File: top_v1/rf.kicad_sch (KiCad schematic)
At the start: 3 parts

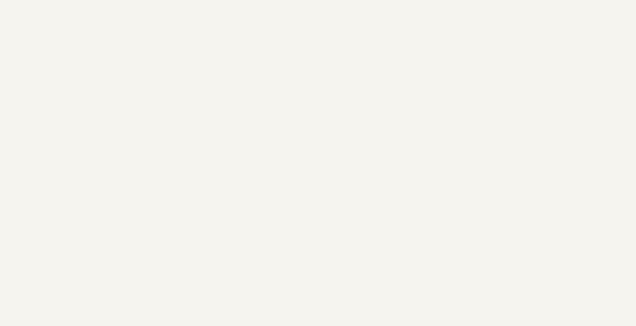
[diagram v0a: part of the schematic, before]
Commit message: File structure enhanced.
Added uniform titleblocks and 3D renders for easier view, file cleanups.
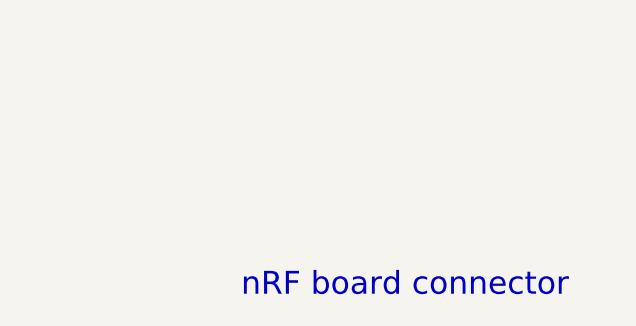
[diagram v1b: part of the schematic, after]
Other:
- note added: "nRF board connector"
- title: (none) -> Top board - nRF and IMU to Nucleo H755ZI
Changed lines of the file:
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@@
 (kicad_sch
-	(version 20231120)
+	(version 20250114)
 	(generator "eeschema")
-	(generator_version "8.0")
+	(generator_version "9.0")
 	(paper "A4")
+	(title_block
+		(title "Top board - nRF and IMU to Nucleo H755ZI")
+		(date "16-12-2024")
+		(rev "1")
+	)
+	(text "nRF board connector"
+		(exclude_from_sim no)
+		(at 209.55 170.18 0)
+		(effects
+			(font
+				(size 2.54 2.54)
+			)
+		)
+	)
 	(junction
 		(at 175.26 81.28)
@@
 	(label "GND"
 		(at 175.26 83.82 0)
-		(fields_autoplaced yes)
 		(effects
 			(font
@@
 		(shape input)
 		(at 164.465 89.535 0)
-		(fields_autoplaced yes)
 		(effects
 			(font
@@
 		(shape input)
 		(at 164.465 86.995 0)
-		(fields_autoplaced yes)
 		(effects
 			(font
@@
 		(shape input)
 		(at 164.465 84.455 0)
-		(fields_autoplaced yes)
 		(effects
 			(font
@@
 		(shape input)
 		(at 184.15 76.2 0)
-		(fields_autoplaced yes)
 		(effects
 			(font
@@
 		(shape input)
 		(at 137.16 81.915 180)
-		(fields_autoplaced yes)
 		(effects
 			(font
@@
 		(shape input)
 		(at 137.16 84.455 180)
-		(fields_autoplaced yes)
 		(effects
 			(font
@@
 		(shape input)
 		(at 137.16 86.995 180)
-		(fields_autoplaced yes)
 		(effects
 			(font
@@
 		(shape input)
 		(at 137.795 89.535 180)
-		(fields_autoplaced yes)
-		(effects
-			(font
+		(effects
+			(font
